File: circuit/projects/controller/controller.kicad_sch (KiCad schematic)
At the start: 50 parts, among them J1 Conn_01x02, SW1 SW_DIP_x01, SW10 SW_DIP_x01, SW2 SW_DIP_x01, SW3 SW_DIP_x01, SW4 SW_DIP_x01, SW5 SW_DIP_x01, SW6 SW_DIP_x01, SW7 SW_DIP_x01, SW8 TOGGLE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

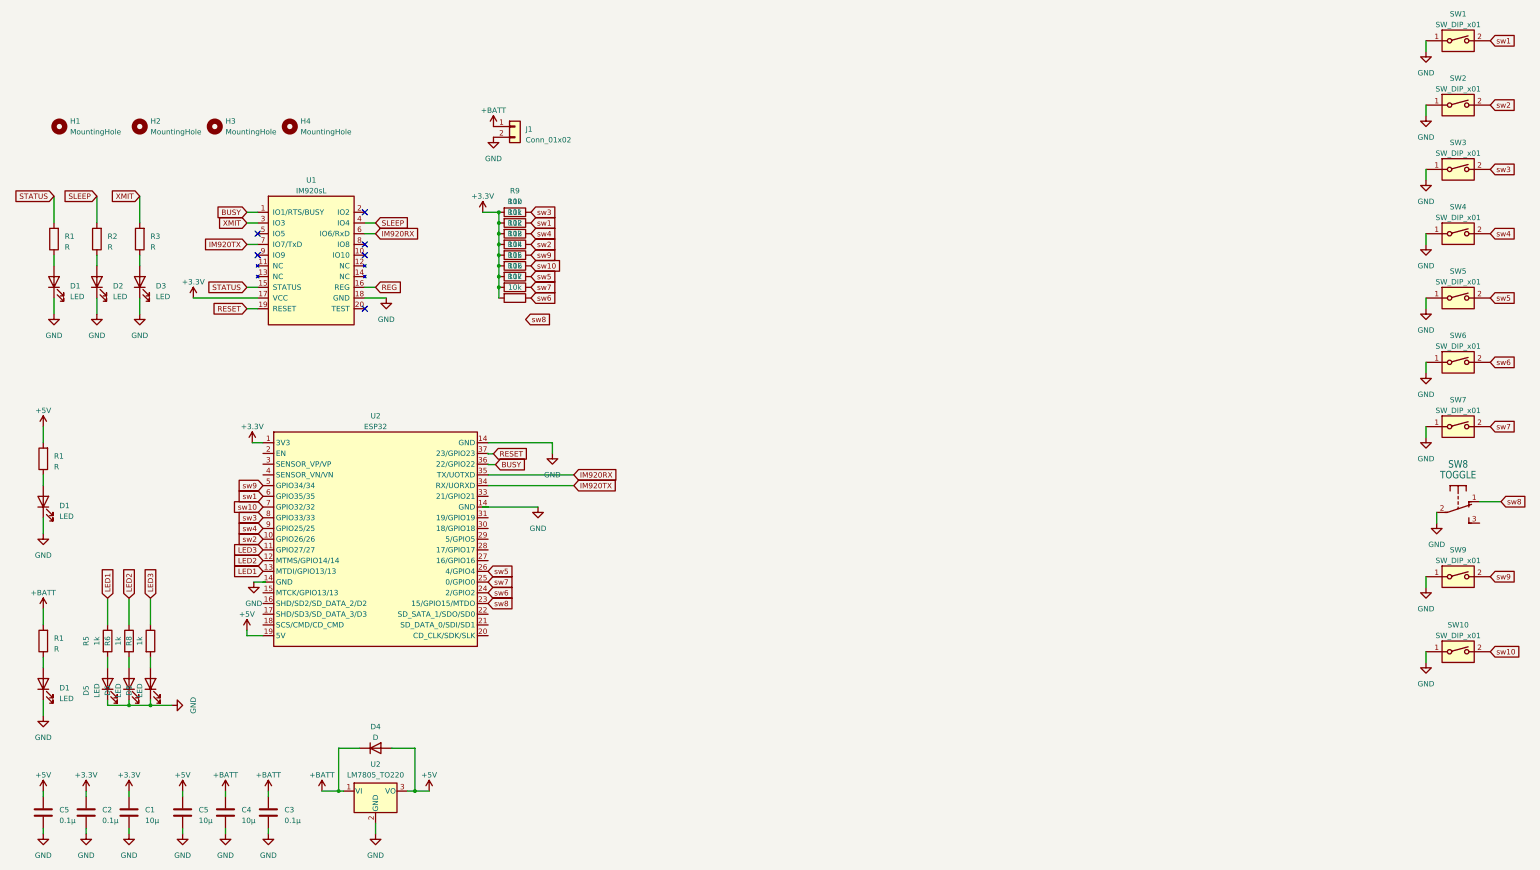
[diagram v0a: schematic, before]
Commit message: ESPのフットプリント違ったので修正します
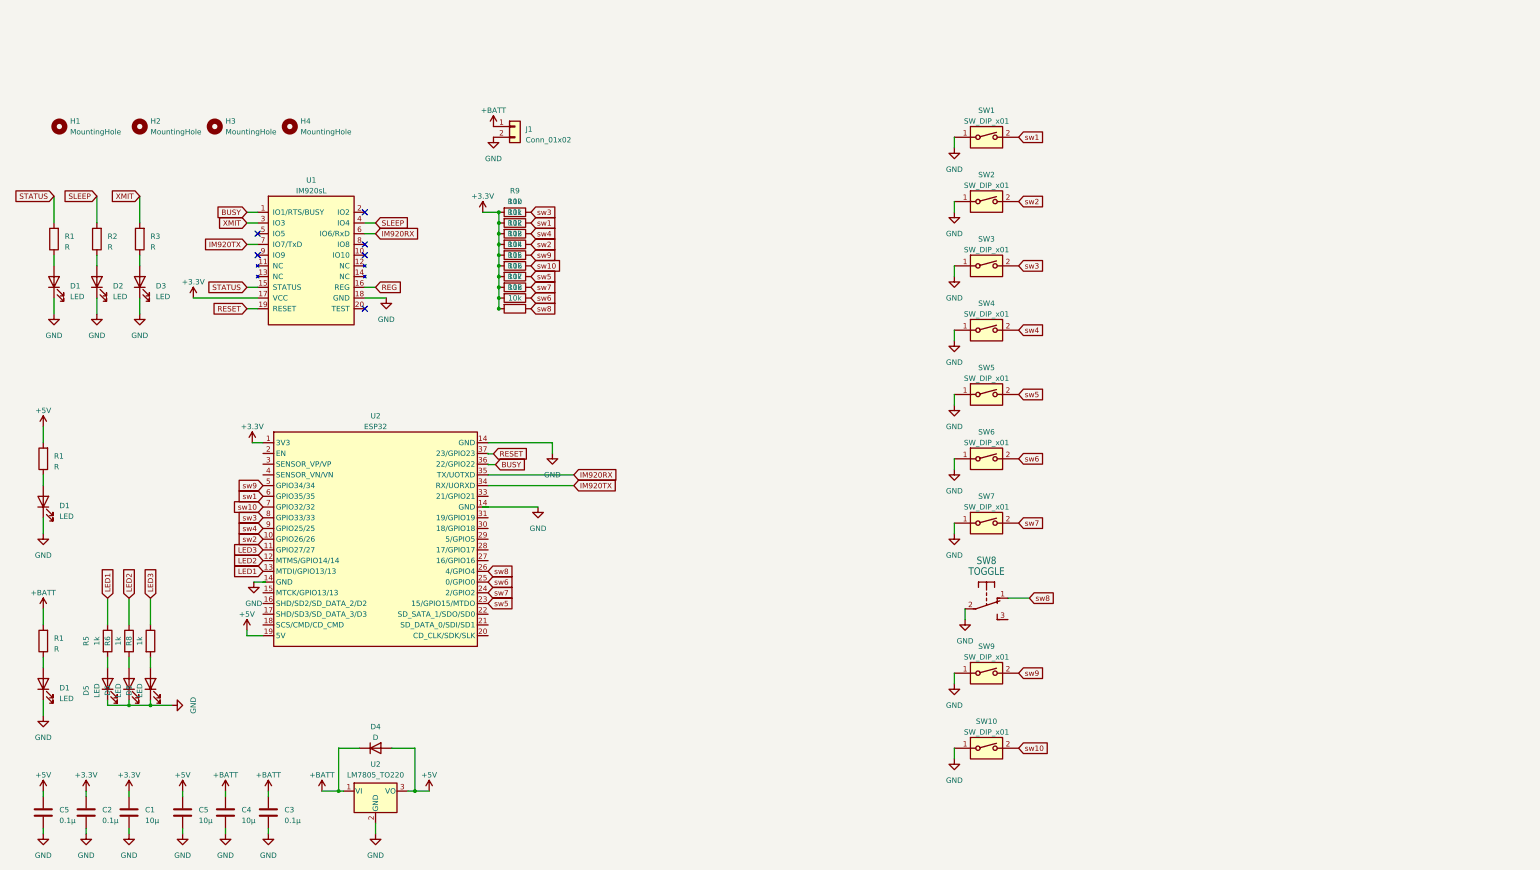
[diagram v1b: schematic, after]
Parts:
- added R18: 10k, Resistor_THT:R_Axial_DIN0204_L3.6mm_D1.6mm_P7.62mm_Horizontal, symbol Device:R
- U2: footprint Boad_dev:ESP32-DevKitC -> ESP32_fot:ESP32
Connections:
- net +3.3V: now also R18.2
- net sw5: now also U2.23 (15/GPIO15/MTDO); no longer U2.26 (4/GPIO4)
- net sw6: now also U2.25 (0/GPIO0); no longer U2.24 (2/GPIO2)
- net sw7: now also U2.24 (2/GPIO2); no longer U2.25 (0/GPIO0)
- net sw8: now also U2.26 (4/GPIO4), R18.1; no longer U2.23 (15/GPIO15/MTDO)
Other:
- moved on the sheet: SW1, SW10, SW2, SW3, SW4, SW5, SW6, SW7, SW8, SW9
